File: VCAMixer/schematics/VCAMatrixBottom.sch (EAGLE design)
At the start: 75 parts, among them IC1 QUAD_OPAMPD, IC2 TL074D, IC4 TL072D, Q1 BC846ALT1SMD, Q10 BSS123, Q2 BC846ALT1SMD, Q3 BC846ALT1SMD, Q4 BC846ALT1SMD, Q5 BC846ALT1SMD, Q6 BC846ALT1SMD, Q7 BC846ALT1SMD, Q8 BC846ALT1SMD, Q9 BSS84

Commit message: more label work
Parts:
- IC2: value TL074D -> QUAD_OPAMPD; device linear:TL074D -> adafruit:QUAD_OPAMPD

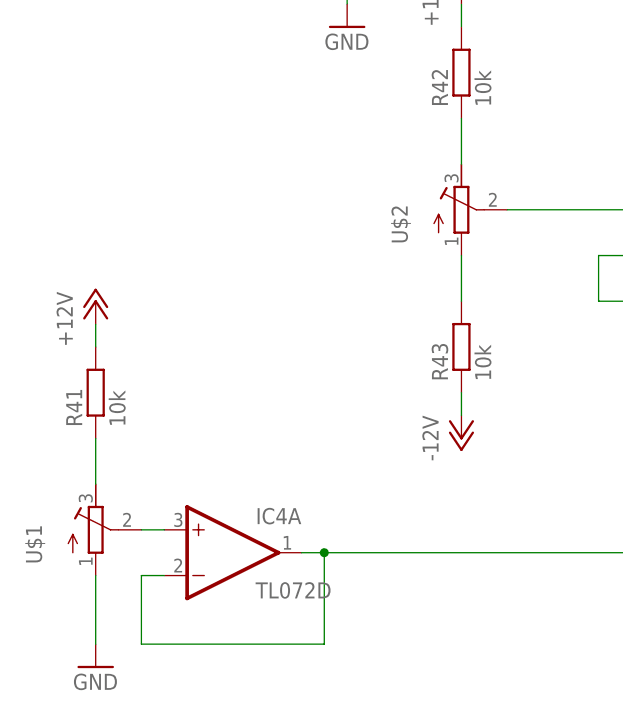
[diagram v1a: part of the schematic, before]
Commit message: finished labelling, named trimpots
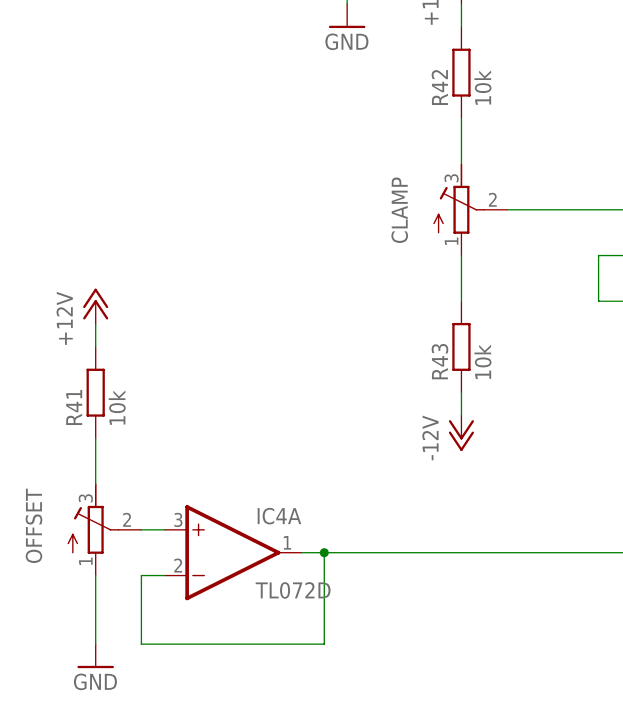
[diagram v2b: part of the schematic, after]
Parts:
- renumbered U$1 to OFFSET, U$2 to CLAMP
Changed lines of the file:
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@@
 <part name="P-5" library="supply1" deviceset="-12V" device=""/>
 <part name="P-6" library="supply1" deviceset="-12V" device=""/>
-<part name="U$1" library="resistor" deviceset="R-TRIMM" device="64W"/>
+<part name="OFFSET" library="resistor" deviceset="R-TRIMM" device="64W"/>
 <part name="P+15" library="supply1" deviceset="+12V" device=""/>
 <part name="GND48" library="supply1" deviceset="GND" device=""/>
@@
 <part name="IC4" library="linear" deviceset="TL072" device="D"/>
 <part name="R41" library="Rebel" deviceset="R-EU_" device="0603" value="10k"/>
-<part name="U$2" library="resistor" deviceset="R-TRIMM" device="64W"/>
+<part name="CLAMP" library="resistor" deviceset="R-TRIMM" device="64W"/>
 <part name="P+17" library="supply1" deviceset="+12V" device=""/>
 <part name="R42" library="Rebel" deviceset="R-EU_" device="0603" value="10k"/>
@@
 <instance part="IC2" gate="C" x="259.08" y="264.16"/>
 <instance part="IC2" gate="D" x="256.54" y="162.56"/>
-<instance part="U$1" gate="G$1" x="-12.7" y="337.82"/>
+<instance part="OFFSET" gate="G$1" x="-12.7" y="337.82"/>
 <instance part="P+15" gate="1" x="-12.7" y="363.22"/>
 <instance part="GND48" gate="1" x="-12.7" y="322.58"/>
@@
 <instance part="IC4" gate="B" x="55.88" y="370.84"/>
 <instance part="R41" gate="G$1" x="-12.7" y="353.06" rot="R90"/>
-<instance part="U$2" gate="G$1" x="27.94" y="373.38"/>
+<instance part="CLAMP" gate="G$1" x="27.94" y="373.38"/>
 <instance part="P+17" gate="1" x="27.94" y="398.78"/>
 <instance part="R42" gate="G$1" x="27.94" y="388.62" rot="R90"/>
@@
 <segment>
 <pinref part="GND48" gate="1" pin="GND"/>
-<pinref part="U$1" gate="G$1" pin="A"/>
+<pinref part="OFFSET" gate="G$1" pin="A"/>
 <wire x1="-12.7" y1="325.12" x2="-12.7" y2="332.74" width="0.1524" layer="91"/>
 </segment>
@@
 <net name="N$33" class="0">
 <segment>
-<pinref part="U$1" gate="G$1" pin="S"/>
+<pinref part="OFFSET" gate="G$1" pin="S"/>
 <wire x1="-7.62" y1="337.82" x2="-5.08" y2="337.82" width="0.1524" layer="91"/>
 <pinref part="IC4" gate="A" pin="+IN"/>
@@
 <net name="N$13" class="0">
 <segment>
-<pinref part="U$1" gate="G$1" pin="E"/>
+<pinref part="OFFSET" gate="G$1" pin="E"/>
 <pinref part="R41" gate="G$1" pin="1"/>
 <wire x1="-12.7" y1="342.9" x2="-12.7" y2="347.98" width="0.1524" layer="91"/>
@@
 <net name="N$44" class="0">
 <segment>
-<pinref part="U$2" gate="G$1" pin="E"/>
+<pinref part="CLAMP" gate="G$1" pin="E"/>
 <pinref part="R42" gate="G$1" pin="1"/>
 <wire x1="27.94" y1="378.46" x2="27.94" y2="383.54" width="0.1524" layer="91"/>
@@
 <net name="N$77" class="0">
 <segment>
-<pinref part="U$2" gate="G$1" pin="A"/>
+<pinref part="CLAMP" gate="G$1" pin="A"/>
 <wire x1="27.94" y1="363.22" x2="27.94" y2="368.3" width="0.1524" layer="91"/>
 <pinref part="R43" gate="G$1" pin="2"/>
@@
 <net name="N$78" class="0">
 <segment>
-<pinref part="U$2" gate="G$1" pin="S"/>
+<pinref part="CLAMP" gate="G$1" pin="S"/>
 <pinref part="IC4" gate="B" pin="+IN"/>
 <wire x1="33.02" y1="373.38" x2="48.26" y2="373.38" width="0.1524" layer="91"/>

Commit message: updated component values and labels
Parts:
- R25, R27, R29, R31, R33, R35, R37, R39: value 20k -> 22k
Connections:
- net N$34 renamed OFFSET_REF
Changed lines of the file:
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@@
 <part name="C8" library="Rebel" deviceset="C-EU" device="C0603K" value="100n"/>
 <part name="C9" library="Rebel" deviceset="C-EU" device="C0603K" value="100n"/>
-<part name="R22" library="Rebel" deviceset="R-EU_" device="0603" value="6k"/>
+<part name="R22" library="Rebel" deviceset="R-EU_" device="0603" value="5k6"/>
 <part name="P+2" library="supply1" deviceset="+12V" device=""/>
 <part name="P+3" library="supply1" deviceset="+12V" device=""/>
@@
 <part name="R24" library="Rebel" deviceset="R-EU_" device="0603" value="100k"/>
 <part name="GND35" library="supply1" deviceset="GND" device=""/>
-<part name="R25" library="Rebel" deviceset="R-EU_" device="0603" value="20k"/>
+<part name="R25" library="Rebel" deviceset="R-EU_" device="0603" value="22k"/>
 <part name="Q1" library="transistor-npn" deviceset="BC846*" device="SMD" technology="ALT1"/>
 <part name="R26" library="Rebel" deviceset="R-EU_" device="0603" value="560"/>
 <part name="P+5" library="supply1" deviceset="+12V" device=""/>
-<part name="R27" library="Rebel" deviceset="R-EU_" device="0603" value="20k"/>
+<part name="R27" library="Rebel" deviceset="R-EU_" device="0603" value="22k"/>
 <part name="Q2" library="transistor-npn" deviceset="BC846*" device="SMD" technology="ALT1"/>
 <part name="R28" library="Rebel" deviceset="R-EU_" device="0603" value="560"/>
 <part name="P+6" library="supply1" deviceset="+12V" device=""/>
-<part name="R29" library="Rebel" deviceset="R-EU_" device="0603" value="20k"/>
+<part name="R29" library="Rebel" deviceset="R-EU_" device="0603" value="22k"/>
 <part name="Q3" library="transistor-npn" deviceset="BC846*" device="SMD" technology="ALT1"/>
 <part name="R30" library="Rebel" deviceset="R-EU_" device="0603" value="560"/>
 <part name="P+7" library="supply1" deviceset="+12V" device=""/>
-<part name="R31" library="Rebel" deviceset="R-EU_" device="0603" value="20k"/>
+<part name="R31" library="Rebel" deviceset="R-EU_" device="0603" value="22k"/>
 <part name="Q4" library="transistor-npn" deviceset="BC846*" device="SMD" technology="ALT1"/>
 <part name="R32" library="Rebel" deviceset="R-EU_" device="0603" value="560"/>
 <part name="P+8" library="supply1" deviceset="+12V" device=""/>
-<part name="R33" library="Rebel" deviceset="R-EU_" device="0603" value="20k"/>
+<part name="R33" library="Rebel" deviceset="R-EU_" device="0603" value="22k"/>
 <part name="Q5" library="transistor-npn" deviceset="BC846*" device="SMD" technology="ALT1"/>
 <part name="R34" library="Rebel" deviceset="R-EU_" device="0603" value="560"/>
 <part name="P+9" library="supply1" deviceset="+12V" device=""/>
-<part name="R35" library="Rebel" deviceset="R-EU_" device="0603" value="20k"/>
+<part name="R35" library="Rebel" deviceset="R-EU_" device="0603" value="22k"/>
 <part name="Q6" library="transistor-npn" deviceset="BC846*" device="SMD" technology="ALT1"/>
 <part name="R36" library="Rebel" deviceset="R-EU_" device="0603" value="560"/>
 <part name="P+10" library="supply1" deviceset="+12V" device=""/>
-<part name="R37" library="Rebel" deviceset="R-EU_" device="0603" value="20k"/>
+<part name="R37" library="Rebel" deviceset="R-EU_" device="0603" value="22k"/>
 <part name="Q7" library="transistor-npn" deviceset="BC846*" device="SMD" technology="ALT1"/>
 <part name="R38" library="Rebel" deviceset="R-EU_" device="0603" value="560"/>
 <part name="P+11" library="supply1" deviceset="+12V" device=""/>
-<part name="R39" library="Rebel" deviceset="R-EU_" device="0603" value="20k"/>
+<part name="R39" library="Rebel" deviceset="R-EU_" device="0603" value="22k"/>
 <part name="Q8" library="transistor-npn" deviceset="BC846*" device="SMD" technology="ALT1"/>
 <part name="R40" library="Rebel" deviceset="R-EU_" device="0603" value="560"/>
@@
 <instances>
 <instance part="IC1" gate="A" x="40.64" y="523.24"/>
-<instance part="P+1" gate="1" x="119.38" y="553.72"/>
+<instance part="P+1" gate="1" x="119.38" y="568.96"/>
 <instance part="P-1" gate="1" x="134.62" y="568.96" rot="R180"/>
 <instance part="GND5" gate="1" x="127" y="568.96" rot="R180"/>
@@
 <pinref part="P+1" gate="1" pin="+12V"/>
 <portref moduleinst="A" port="+12V"/>
+<wire x1="119.38" y1="566.42" x2="119.38" y2="551.18" width="0.1524" layer="91"/>
 </segment>
 <segment>
@@
 </segment>
 </net>
-<net name="N$34" class="0">
+<net name="OFFSET_REF" class="0">
 <segment>
 <wire x1="-5.08" y1="332.74" x2="-7.62" y2="332.74" width="0.1524" layer="91"/>

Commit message: Updated Bottom Board
New I-to-V configuration and LED Drivers, also includes work in progress
.brd file
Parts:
- removed Q8: BC846ALT1SMD, transistor-npn:BC846ALT1SMD
- removed R10, R13, R14, R15, R16, R20, R21, R22, R5, R6, R8, R9: 100k, Rebel:R-EU_0603
- added C10: 100n, resistor:C-EUC0603K
- added C11: 4u7, resistor:C-EUC0603K
- added C12, C7, C8, C9: 100p, resistor:C-EUC0603K
- added C13, C14: 100n, Rebel:C-EUC0603K
- added IC5: QUAD_OPAMPD, adafruit:QUAD_OPAMPD
- added Q11: BC856ALT1SMD, transistor-pnp:BC856ALT1SMD
- added R48, R51, R52, R53, R54, R55: 4k7, Rebel:R-EU_0603
- added R49: 100k, Rebel:R-EU_0603
- added R50: 22k, Rebel:R-EU_0603
- added R56, R57, R58, R59: 30k, Rebel:R-EU_0603
- Q1, Q2, Q3, Q4, Q5, Q6, Q7: value BC846ALT1SMD -> BC856ALT1SMD; device transistor-npn:BC846ALT1SMD -> transistor-pnp:BC856ALT1SMD
- R25, R27, R29, R31, R37, R39: value 22k -> 100k
- R26, R28, R30, R32, R38, R40: value 560 -> 22k
- R33: value 22k -> 4k7
- R34: value 560 -> 100k
- R36: value 560 -> 4k7
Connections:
- removed net CV_A: R13.2
- removed net CV_D: R8.2
- removed net IC2_1: R10.1, R20.1
- removed net IC2_2: R10.2, R8.1
- removed net IC2_3: R15.1, R9.1
- removed net IC2_5: R13.1, R15.2
- removed net IC2_6: R14.1, R21.1
- removed net N$20: R10.1
- removed net N$28: R13.1
- removed net N$29: R14.1
- removed net N$30: R15.1
- removed net N$31: R16.1
- removed net N$39: R19.1
- removed net N$40: R20.1
- removed net N$41: R21.1
- removed net N$42: R22.1
- removed net N$45: Q6.B, R35.2
- removed net N$46: Q2.B, R27.2
- removed net N$49: IC2C.OUT, Q2.E, R28.1, R36.1
- removed net N$51: Q3.B, R29.2
- removed net N$53: Q3.E, R30.1
- removed net N$54: Q6.E, R36.1
- removed net N$56: Q4.B, R31.2
- removed net N$58: IC2A.-IN, R13.2, R19.2, R2.2, R3.2, R7.1
- removed net N$60: Q4.E, R32.1
- removed net N$61: Q7.B, R37.2
- removed net N$62: Q5.B, R33.2
- removed net N$64: Q5.E, R34.1
- removed net N$66: Q7.E, R38.1
- removed net N$67: Q8.B, R39.2
- new net N$15: Q6.B, R37.2, R38.2
- new net N$16: Q7.B, R39.2, R40.2
- net +12V: now also C13.1, C14.1, C8.1, IC5P.V+, R33.2, R36.2, R48.2, R51.2, R52.2, R53.2, R54.2, R55.2; no longer Q1.C, Q2.C, Q3.C, Q4.C, Q5.C, Q6.C, Q7.C, Q8.C, R22.2
- net -12V: now also C13.1, C14.1, C9.2, IC5P.V-
- net AUDIO_IN: no longer R16.1
- net GND: now also C10.2, C11.2, C13.2, C14.2, C8.2, C9.1, IC5A.+IN, IC5B.+IN, IC5C.+IN, IC5D.+IN, Q1.C, Q11.C, Q2.C, Q3.C, Q4.C, Q5.C, Q6.C, Q7.C, R26.1, R28.1, R30.1, R32.1, R35.1, R38.1, R40.1, R50.1
- net IC2_7: no longer R21.2
- net LED_1: now also Q1.E, R33.1; no longer R26.2
- net LED_2: now also Q2.E, R53.1; no longer R28.2
- net LED_3: now also Q3.E, R54.1; no longer R30.2
- net LED_4: now also Q4.E, R55.1; no longer R32.2
- net LED_5: now also Q11.E, R51.1; no longer R34.2
- net LED_6: now also Q5.E, R36.1; no longer R36.2
- net LED_7: now also Q6.E, R48.1; no longer R38.2
- net LED_8: now also Q7.E, R52.1; no longer R40.2
- net N$1: no longer R9.2
- net N$10: now also C9.2, IC5B.-IN, R59.1; no longer R6.1
- net N$11: now also R4.2; no longer R15.2, R21.2, R5.2, R9.2
- net N$12: now also Q11.B, R49.2, R50.2; no longer R16.2
- net N$13: no longer IC2B.OUT, R18.1
- net N$14: now also Q5.B, R34.2, R35.2; no longer R20.2
- net N$17: no longer R2.1, R22.1
- net N$18: now also C7.2, IC5D.-IN, R57.1; no longer R8.1
- net N$19: no longer R9.1
- net N$2: no longer R5.1
- net N$21: now also Q3.B, R29.2, R30.2; no longer Q1.B, R25.2
- net N$24: now also Q4.B, R31.2, R32.2; no longer Q8.E, R40.1
- net N$33: now also C10.1
- net N$4: now also Q1.B, R25.2, R26.2; no longer Q1.E, R26.1, R5.2
- net N$47: now also R19.2; no longer R10.2, R16.2, R22.2, R6.2
- net N$59: now also R2.2; no longer R14.2, R20.2, R4.2, R8.2
- net N$6: now also Q2.B, R27.2, R28.2; no longer C2.2, IC2D.OUT, R6.1
- net N$7: now also IC2A.-IN, R3.2, R7.1; no longer R14.2, R3.1
- net N$78: now also C11.1
- net N$8: now also C8.2, IC5A.-IN, R58.1; no longer R4.1
- net N$9: now also C12.2, IC5C.-IN, R56.1; no longer C4.2, IC2A.OUT, R12.1, R5.1
- net OUTPUT_A: now also R49.1; no longer R33.1
- net OUTPUT_B: now also R34.1; no longer R35.1
- net OUT_A: now also C8.1, IC2A.OUT, IC5A.OUT, R3.1, R58.2; no longer C4.1, R12.2
- net OUT_B: now also C9.1, IC2B.OUT, IC5B.OUT, R2.1, R59.2; no longer R18.2
- net OUT_C: now also C12.1, IC2C.OUT, IC5C.OUT, R4.1, R56.2; no longer R36.2
- net OUT_D: now also C7.1, IC2D.OUT, IC5D.OUT, R19.1, R57.2; no longer C2.1, R6.2
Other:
- moved on the sheet: C1, C2, C3, C4, C5, C6, IC1C, IC2A, IC2B, IC2C, IC2D, IC4A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

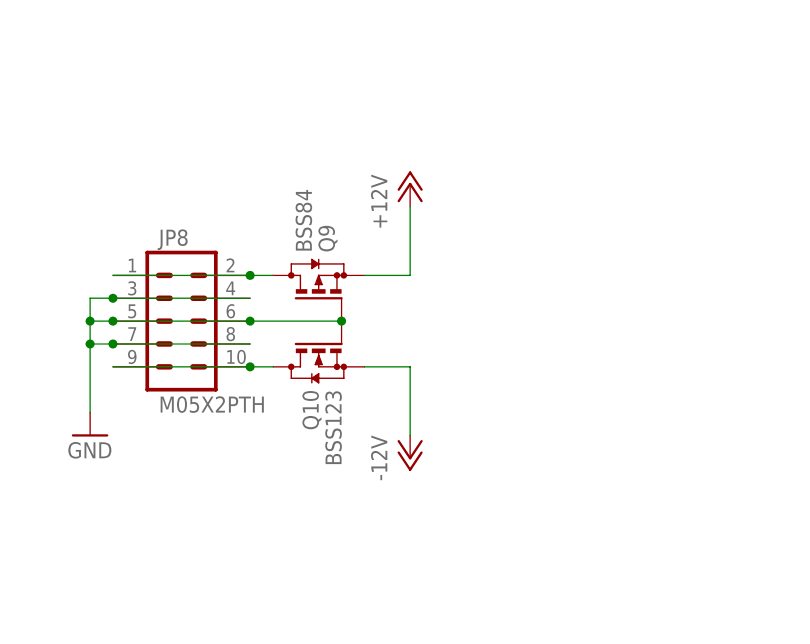
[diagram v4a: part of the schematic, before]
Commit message: Completed Rev 2 of VCA Matrix
Updated Bottom Board
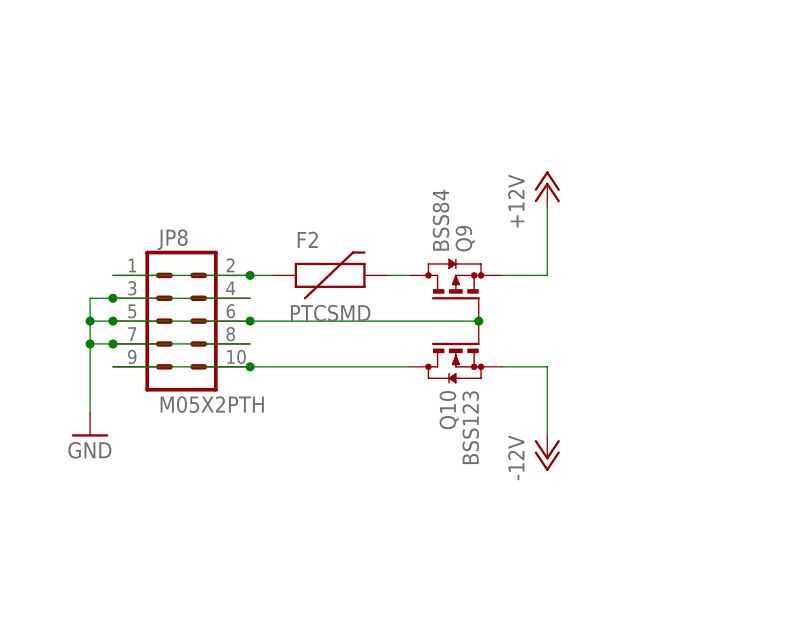
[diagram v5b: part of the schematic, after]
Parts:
- added F2: PTCSMD, SparkFun:PTCSMD
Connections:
- net N$17: now also F2.2, Q9.D
- net N$79: now also F2.1; no longer Q9.D
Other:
- moved on the sheet: Q10, Q9
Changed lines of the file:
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@@
 <?xml version="1.0" encoding="utf-8"?>
 <!DOCTYPE eagle SYSTEM "eagle.dtd">
-<eagle version="7.6.0">
+<eagle version="8.0.0">
 <drawing>
 <settings>
@@
 <part name="GND20" library="supply1" deviceset="GND" device=""/>
 <part name="P-10" library="supply1" deviceset="-12V" device=""/>
+<part name="F2" library="SparkFun" deviceset="PTC" device="SMD"/>
 </parts>
 <sheets>
@@
 <instance part="GND49" gate="1" x="452.12" y="548.64"/>
 <instance part="IC4" gate="P" x="444.5" y="548.64"/>
-<instance part="P+18" gate="1" x="436.88" y="472.44"/>
+<instance part="P+18" gate="1" x="452.12" y="472.44"/>
 <instance part="GND60" gate="1" x="401.32" y="444.5"/>
-<instance part="P-9" gate="1" x="436.88" y="441.96"/>
+<instance part="P-9" gate="1" x="452.12" y="441.96"/>
 <instance part="JP8" gate="G$1" x="411.48" y="457.2"/>
-<instance part="Q9" gate="G$1" x="426.72" y="462.28" rot="MR90">
-<attribute name="OC_FARNELL" x="426.72" y="462.28" size="1.778" layer="96" rot="MR90" display="off"/>
+<instance part="Q9" gate="G$1" x="441.96" y="462.28" rot="MR90">
+<attribute name="OC_FARNELL" x="441.96" y="462.28" size="1.778" layer="96" rot="MR90" display="off"/>
 </instance>
-<instance part="Q10" gate="G$1" x="426.72" y="452.12" rot="MR270">
-<attribute name="OC_FARNELL" x="426.72" y="452.12" size="1.778" layer="96" rot="MR270" display="off"/>
+<instance part="Q10" gate="G$1" x="441.96" y="452.12" rot="MR270">
+<attribute name="OC_FARNELL" x="441.96" y="452.12" size="1.778" layer="96" rot="MR270" display="off"/>
 </instance>
 <instance part="J3" gate="G$1" x="431.8" y="398.78" rot="MR0"/>
@@
 <instance part="GND20" gate="1" x="477.52" y="523.24"/>
 <instance part="P-10" gate="1" x="467.36" y="520.7"/>
+<instance part="F2" gate="G$1" x="426.72" y="462.28"/>
 </instances>
 <busses>
@@
 <pinref part="JP8" gate="G$1" pin="3"/>
 <pinref part="Q9" gate="G$1" pin="G"/>
-<wire x1="419.1" y1="457.2" x2="429.26" y2="457.2" width="0.1524" layer="91"/>
+<wire x1="419.1" y1="457.2" x2="444.5" y2="457.2" width="0.1524" layer="91"/>
 <pinref part="Q10" gate="G$1" pin="G"/>
-<junction x="429.26" y="457.2"/>
+<junction x="444.5" y="457.2"/>
 <junction x="419.1" y="457.2"/>
 </segment>
@@
 <segment>
 <pinref part="Q9" gate="G$1" pin="S"/>
-<wire x1="431.8" y1="462.28" x2="436.88" y2="462.28" width="0.1524" layer="91"/>
-<wire x1="436.88" y1="462.28" x2="436.88" y2="469.9" width="0.1524" layer="91"/>
+<wire x1="447.04" y1="462.28" x2="452.12" y2="462.28" width="0.1524" layer="91"/>
+<wire x1="452.12" y1="462.28" x2="452.12" y2="469.9" width="0.1524" layer="91"/>
 <pinref part="P+18" gate="1" pin="+12V"/>
 </segment>
@@
 <pinref part="P-9" gate="1" pin="-12V"/>
 <pinref part="Q10" gate="G$1" pin="S"/>
-<wire x1="431.8" y1="452.12" x2="436.88" y2="452.12" width="0.1524" layer="91"/>
-<wire x1="436.88" y1="444.5" x2="436.88" y2="452.12" width="0.1524" layer="91"/>
+<wire x1="447.04" y1="452.12" x2="452.12" y2="452.12" width="0.1524" layer="91"/>
+<wire x1="452.12" y1="444.5" x2="452.12" y2="452.12" width="0.1524" layer="91"/>
 </segment>
 <segment>
@@
 <pinref part="JP8" gate="G$1" pin="9"/>
 <pinref part="Q10" gate="G$1" pin="D"/>
-<wire x1="419.1" y1="452.12" x2="421.64" y2="452.12" width="0.1524" layer="91"/>
+<wire x1="419.1" y1="452.12" x2="436.88" y2="452.12" width="0.1524" layer="91"/>
 <junction x="419.1" y="452.12"/>
 </segment>
@@
 <pinref part="JP8" gate="G$1" pin="2"/>
 <pinref part="JP8" gate="G$1" pin="1"/>
-<pinref part="Q9" gate="G$1" pin="D"/>
+<pinref part="F2" gate="G$1" pin="1"/>
 <wire x1="419.1" y1="462.28" x2="421.64" y2="462.28" width="0.1524" layer="91"/>
 <junction x="419.1" y="462.28"/>
@@
 </segment>
 </net>
+<net name="N$17" class="0">
+<segment>
+<pinref part="F2" gate="G$1" pin="2"/>
+<pinref part="Q9" gate="G$1" pin="D"/>
+<wire x1="434.34" y1="462.28" x2="436.88" y2="462.28" width="0.1524" layer="91"/>
+</segment>
+</net>

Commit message: Updated Net Names
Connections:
- new net ITOV_A: C8.1, IC5A.OUT, R3.1, R58.2
- new net ITOV_B: C9.1, IC5B.OUT, R2.1, R59.2
- new net ITOV_C: C12.1, IC5C.OUT, R4.1, R56.2
- new net ITOV_D: C7.1, IC5D.OUT, R19.1, R57.2
- net OUTPUT_A: now also J4.5, R44.1; no longer IC2A.OUT, R44.2, R49.1, R7.2
- net OUTPUT_B: now also J4.4, R47.1; no longer IC2B.OUT, R11.2, R34.1, R47.2
- net OUTPUT_C: now also J4.2, R45.1; no longer IC2C.OUT, R17.2, R37.1, R45.2
- net OUTPUT_D: now also J4.1, R46.1; no longer IC2D.OUT, R23.2, R39.1, R46.2
- net OUT_A: now also R44.2, R49.1, R7.2; no longer C8.1, IC5A.OUT, J4.5, R3.1, R44.1, R58.2
- net OUT_B: now also R11.2, R34.1, R47.2; no longer C9.1, IC5B.OUT, J4.4, R2.1, R47.1, R59.2
- net OUT_C: now also R17.2, R37.1, R45.2; no longer C12.1, IC5C.OUT, J4.2, R4.1, R45.1, R56.2
- net OUT_D: now also R23.2, R39.1, R46.2; no longer C7.1, IC5D.OUT, J4.1, R19.1, R46.1, R57.2

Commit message: updated routing
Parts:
- C10: value 100n -> 4u7
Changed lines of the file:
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@@
 <?xml version="1.0" encoding="utf-8"?>
 <!DOCTYPE eagle SYSTEM "eagle.dtd">
-<eagle version="8.0.2">
+<eagle version="7.5.0">
 <drawing>
 <settings>
@@
 <part name="R59" library="Rebel" deviceset="R-EU_" device="0603" value="30k"/>
 <part name="C9" library="resistor" deviceset="C-EU" device="C0603K" value="100p"/>
-<part name="C10" library="resistor" deviceset="C-EU" device="C0603K" value="100n"/>
+<part name="C10" library="resistor" deviceset="C-EU" device="C0603K" value="4u7"/>
 <part name="C11" library="resistor" deviceset="C-EU" device="C0603K" value="4u7"/>
 <part name="GND18" library="supply1" deviceset="GND" device=""/>
